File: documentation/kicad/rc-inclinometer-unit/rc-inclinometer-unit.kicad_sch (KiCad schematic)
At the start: 1 part

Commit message: kicad schema update
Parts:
- added SW?: SW_DIP_x01, symbol Switch:SW_DIP_x01
- added U?: Winch controller, symbol rc-inclinometer-unit-custom-library:Winch controller
- added U?: Logic Level Converter, symbol rc-inclinometer-unit-custom-library:Logic Level Converter
- added U?: Passive buzzer module, symbol rc-inclinometer-unit-custom-library:Passive buzzer module
- added U?: RC Receiver, symbol rc-inclinometer-unit-custom-library:RC Receiver
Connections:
- net at U?.12 (~{D9}): now also U?. (VCC)
- net at U?.4 (GND): now also SW?.2, U?. (LV4)
- net at U?.5 (D2): now also SW?.1
- net at U?.8 (~{D5}): now also U?. (LV4)
- net +5V: no longer names the net of U?.30 (VIN)
- net +5V: now also U?. (GND), U?. (VCC)
- net GND: no longer names the net of U?.29 (GND)
- net GND: now also U?. (GND), U?. (VCC), U?. (VCC)
- net IO: no longer names the net of U?.6 (~{D3})
- net IO: now also U?. (VCC)
- net VCC: no longer names the net of U?.17 (3V3)
- net VCC: now also U?. (LV4), U?. (VCC)
- new net: U?. (GND), U?. (LV4) (x3)
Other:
- note removed: "Passive buzzer module"
- note removed: "RC Receiver"

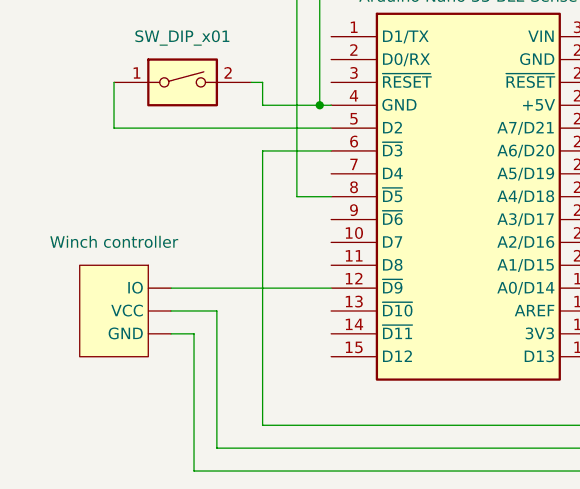
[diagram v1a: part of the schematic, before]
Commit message: front dig servo schema
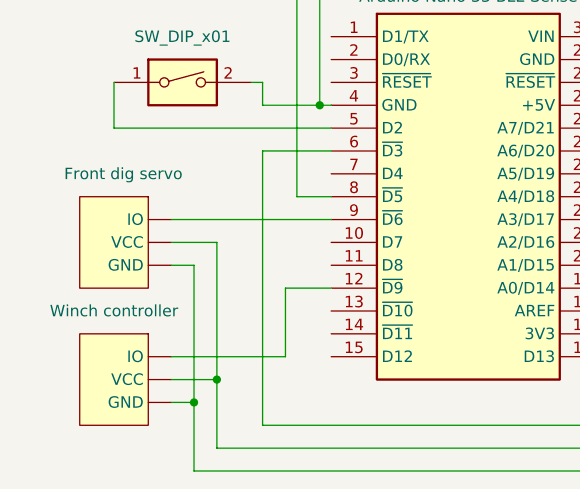
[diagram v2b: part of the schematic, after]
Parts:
- added U?: Front dig servo, symbol rc-inclinometer-unit-custom-library:Winch controller
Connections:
- net at U?. (GND), U?. (VCC), U?.30 (VIN): now also U?. (VCC)
- net at U?.9 (~{D6}): now also U?. (VCC)
- net at U?. (LV4): now also U?. (GND)
- net at U?. (GND): no longer U?. (LV4)
- new net: U?. (LV4), U?. (VCC), U?.17 (3V3)
- new net: U?. (GND), U?. (VCC), U?. (VCC), U?. (VCC), U?.29 (GND)
- new net: U?. (GND), U?. (LV4) (x2)
- now unconnected: U?. (GND), U?. (GND), U?. (GND)
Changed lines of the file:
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@@
   (junction (at 191.77 73.66) (diameter 0) (color 0 0 0 0)
   )
+  (junction (at 111.76 111.76) (diameter 0) (color 0 0 0 0)
+  )
   (junction (at 125.73 78.74) (diameter 0) (color 0 0 0 0)
   )
   (junction (at 189.23 71.12) (diameter 0) (color 0 0 0 0)
   )
+  (junction (at 114.3 109.22) (diameter 0) (color 0 0 0 0)
+  )
   (junction (at 161.29 104.14) (diameter 0) (color 0 0 0 0)
   )
@@
     (stroke (width 0) (type default) (color 0 0 0 0))
   )
-  (wire (pts (xy 109.22 101.6) (xy 114.3 101.6))
-    (stroke (width 0) (type default) (color 0 0 0 0))
-  )
   (wire (pts (xy 163.83 88.9) (xy 171.45 88.9))
     (stroke (width 0) (type default) (color 0 0 0 0))
@@
     (stroke (width 0) (type default) (color 0 0 0 0))
   )
-  (wire (pts (xy 114.3 101.6) (xy 114.3 116.84))
+  (wire (pts (xy 109.22 109.22) (xy 114.3 109.22))
+    (stroke (width 0) (type default) (color 0 0 0 0))
+  )
+  (wire (pts (xy 114.3 116.84) (xy 114.3 109.22))
+    (stroke (width 0) (type default) (color 0 0 0 0))
+  )
+  (wire (pts (xy 109.22 96.52) (xy 111.76 96.52))
     (stroke (width 0) (type default) (color 0 0 0 0))
   )
@@
     (stroke (width 0) (type default) (color 0 0 0 0))
   )
+  (wire (pts (xy 109.22 93.98) (xy 114.3 93.98))
+    (stroke (width 0) (type default) (color 0 0 0 0))
+  )
+  (wire (pts (xy 114.3 109.22) (xy 114.3 93.98))
+    (stroke (width 0) (type default) (color 0 0 0 0))
+  )
+  (wire (pts (xy 121.92 99.06) (xy 121.92 106.68))
+    (stroke (width 0) (type default) (color 0 0 0 0))
+  )
   (wire (pts (xy 191.77 73.66) (xy 193.04 73.66))
     (stroke (width 0) (type default) (color 0 0 0 0))
   )
+  (wire (pts (xy 127 99.06) (xy 121.92 99.06))
+    (stroke (width 0) (type default) (color 0 0 0 0))
+  )
   (wire (pts (xy 157.48 104.14) (xy 161.29 104.14))
     (stroke (width 0) (type default) (color 0 0 0 0))
@@
     (stroke (width 0) (type default) (color 0 0 0 0))
   )
-  (wire (pts (xy 109.22 104.14) (xy 111.76 104.14))
+  (wire (pts (xy 109.22 111.76) (xy 111.76 111.76))
     (stroke (width 0) (type default) (color 0 0 0 0))
   )
@@
     (stroke (width 0) (type default) (color 0 0 0 0))
   )
+  (wire (pts (xy 109.22 91.44) (xy 127 91.44))
+    (stroke (width 0) (type default) (color 0 0 0 0))
+  )
   (wire (pts (xy 189.23 55.88) (xy 182.88 55.88))
     (stroke (width 0) (type default) (color 0 0 0 0))
@@
     (stroke (width 0) (type default) (color 0 0 0 0))
   )
-  (wire (pts (xy 109.22 99.06) (xy 127 99.06))
-    (stroke (width 0) (type default) (color 0 0 0 0))
-  )
   (wire (pts (xy 191.77 60.96) (xy 191.77 50.8))
     (stroke (width 0) (type default) (color 0 0 0 0))
   )
-  (wire (pts (xy 111.76 104.14) (xy 111.76 119.38))
+  (wire (pts (xy 109.22 106.68) (xy 121.92 106.68))
+    (stroke (width 0) (type default) (color 0 0 0 0))
+  )
+  (wire (pts (xy 111.76 111.76) (xy 111.76 119.38))
+    (stroke (width 0) (type default) (color 0 0 0 0))
+  )
+  (wire (pts (xy 111.76 111.76) (xy 111.76 96.52))
     (stroke (width 0) (type default) (color 0 0 0 0))
   )
@@
     (pin "9")
   )
+  (symbol (lib_id "rc-inclinometer-unit-custom-library:Winch controller") (at 102.87 86.36 0) (mirror y) (unit 1)
+    (in_bom yes) (on_board yes)
+    (property "Reference" "U?" (id 0) (at 102.87 83.82 0)
+      (effects (font (size 1.27 1.27)) hide)
+    )
+    (property "Value" "Front dig servo" (id 1) (at 110.49 86.36 0)
+      (effects (font (size 1.27 1.27)) (justify left))
+    )
+    (property "Footprint" "" (id 2) (at 102.87 86.36 0)
+      (effects (font (size 1.27 1.27)) hide)
+    )
+    (property "Datasheet" "" (id 3) (at 102.87 86.36 0)
+      (effects (font (size 1.27 1.27)) hide)
+    )
+    (pin "")
+    (pin "")
+    (pin "")
+  )
   (symbol (lib_id "Switch:SW_DIP_x01") (at 110.49 76.2 0) (unit 1)
     (in_bom yes) (on_board yes) (fields_autoplaced)
@@
     (pin "2")
   )
-  (symbol (lib_id "rc-inclinometer-unit-custom-library:Winch controller") (at 102.87 93.98 0) (mirror y) (unit 1)
+  (symbol (lib_id "rc-inclinometer-unit-custom-library:Winch controller") (at 102.87 101.6 0) (mirror y) (unit 1)
     (in_bom yes) (on_board yes) (fields_autoplaced)
-    (property "Reference" "U?" (id 0) (at 102.87 91.44 0)
-      (effects (font (size 1.27 1.27)) hide)
-    )
-    (property "Value" "Winch controller" (id 1) (at 102.87 93.98 0))
-    (property "Footprint" "" (id 2) (at 102.87 93.98 0)
-      (effects (font (size 1.27 1.27)) hide)
-    )
-    (property "Datasheet" "" (id 3) (at 102.87 93.98 0)
+    (property "Reference" "U?" (id 0) (at 102.87 99.06 0)
+      (effects (font (size 1.27 1.27)) hide)
+    )
+    (property "Value" "Winch controller" (id 1) (at 102.87 101.6 0))
+    (property "Footprint" "" (id 2) (at 102.87 101.6 0)
+      (effects (font (size 1.27 1.27)) hide)
+    )
+    (property "Datasheet" "" (id 3) (at 102.87 101.6 0)
       (effects (font (size 1.27 1.27)) hide)
     )
@@
       (reference "U?") (unit 1) (value "Arduino Nano 33 BLE Sense") (footprint "Arduino:Arduino_Nano")
     )
+    (path "/2419fd11-7a3e-44cd-918f-8db3ea424502"
+      (reference "U?") (unit 1) (value "Front dig servo") (footprint "")
+    )
     (path "/7751ee78-6f34-4432-a4ed-c73af0d92627"

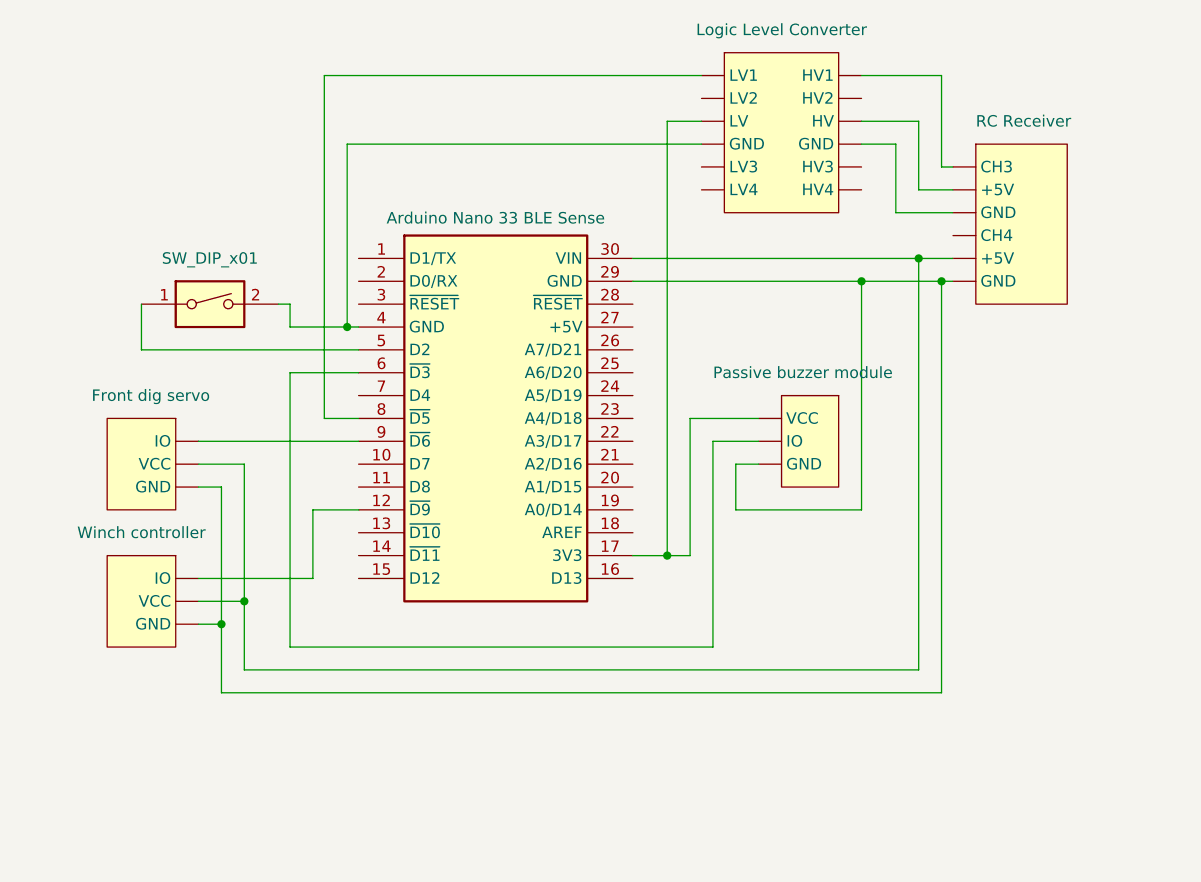
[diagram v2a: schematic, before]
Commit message: measure speed with hall effect sensor
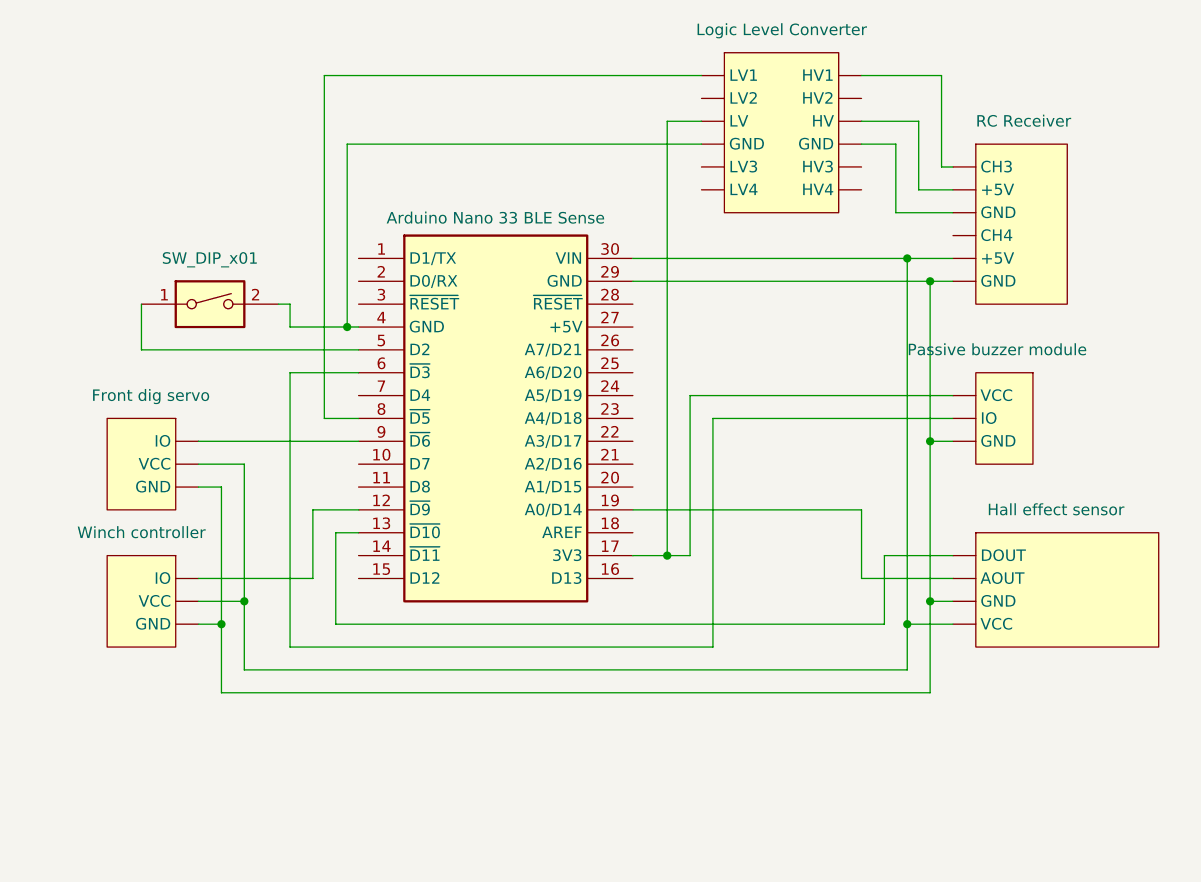
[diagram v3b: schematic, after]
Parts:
- added U?: Hall effect sensor, symbol rc-inclinometer-unit-custom-library:Hall effect sensor
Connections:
- net at U?.13 (~{D10}): now also U?. (VCC)
- net at U?.19 (A0/D14): now also U?. (VCC)
- net at U?. (GND), U?. (VCC), U?. (VCC)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: now also U?. (VCC)
- net at U?. (LV4): now also U?. (GND)
- net at U?. (GND): no longer U?. (LV4)
- new net: U?. (LV4), U?. (VCC), U?.17 (3V3)
- new net: U?. (GND), U?. (VCC), U?. (VCC), U?. (VCC), U?. (VCC), U?.29 (GND)
- new net: U?. (GND), U?. (LV4) (x2)
- now unconnected: U?. (GND), U?. (GND), U?. (GND)
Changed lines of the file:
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@@
 (kicad_sch (version 20211123) (generator eeschema)
   (paper "A4")
-  (junction (at 182.88 73.66) (diameter 0) (color 0 0 0 0)
-  )
-  (junction (at 191.77 73.66) (diameter 0) (color 0 0 0 0)
+  (junction (at 187.96 71.12) (diameter 0) (color 0 0 0 0)
   )
   (junction (at 111.76 111.76) (diameter 0) (color 0 0 0 0)
   )
+  (junction (at 190.5 73.66) (diameter 0) (color 0 0 0 0)
+  )
   (junction (at 125.73 78.74) (diameter 0) (color 0 0 0 0)
   )
-  (junction (at 189.23 71.12) (diameter 0) (color 0 0 0 0)
-  )
   (junction (at 114.3 109.22) (diameter 0) (color 0 0 0 0)
   )
+  (junction (at 187.96 111.76) (diameter 0) (color 0 0 0 0)
+  )
   (junction (at 161.29 104.14) (diameter 0) (color 0 0 0 0)
   )
+  (junction (at 190.5 109.22) (diameter 0) (color 0 0 0 0)
+  )
+  (junction (at 190.5 91.44) (diameter 0) (color 0 0 0 0)
+  )
+  (wire (pts (xy 157.48 99.06) (xy 182.88 99.06))
+    (stroke (width 0) (type default) (color 0 0 0 0))
+  )
   (wire (pts (xy 119.38 78.74) (xy 119.38 76.2))
     (stroke (width 0) (type default) (color 0 0 0 0))
   )
-  (wire (pts (xy 163.83 88.9) (xy 171.45 88.9))
-    (stroke (width 0) (type default) (color 0 0 0 0))
-  )
-  (wire (pts (xy 182.88 73.66) (xy 182.88 99.06))
-    (stroke (width 0) (type default) (color 0 0 0 0))
-  )
   (wire (pts (xy 182.88 50.8) (xy 191.77 50.8))
     (stroke (width 0) (type default) (color 0 0 0 0))
@@
     (stroke (width 0) (type default) (color 0 0 0 0))
   )
+  (wire (pts (xy 187.96 71.12) (xy 193.04 71.12))
+    (stroke (width 0) (type default) (color 0 0 0 0))
+  )
   (wire (pts (xy 161.29 104.14) (xy 163.83 104.14))
     (stroke (width 0) (type default) (color 0 0 0 0))
   )
-  (wire (pts (xy 189.23 71.12) (xy 193.04 71.12))
+  (wire (pts (xy 157.48 71.12) (xy 187.96 71.12))
+    (stroke (width 0) (type default) (color 0 0 0 0))
+  )
+  (wire (pts (xy 187.96 111.76) (xy 187.96 116.84))
+    (stroke (width 0) (type default) (color 0 0 0 0))
+  )
+  (wire (pts (xy 111.76 119.38) (xy 190.5 119.38))
     (stroke (width 0) (type default) (color 0 0 0 0))
   )
@@
     (stroke (width 0) (type default) (color 0 0 0 0))
   )
+  (wire (pts (xy 187.96 111.76) (xy 193.04 111.76))
+    (stroke (width 0) (type default) (color 0 0 0 0))
+  )
+  (wire (pts (xy 190.5 73.66) (xy 193.04 73.66))
+    (stroke (width 0) (type default) (color 0 0 0 0))
+  )
   (wire (pts (xy 109.22 96.52) (xy 111.76 96.52))
     (stroke (width 0) (type default) (color 0 0 0 0))
   )
-  (wire (pts (xy 189.23 71.12) (xy 189.23 116.84))
-    (stroke (width 0) (type default) (color 0 0 0 0))
-  )
-  (wire (pts (xy 191.77 73.66) (xy 191.77 119.38))
+  (wire (pts (xy 182.88 99.06) (xy 182.88 106.68))
+    (stroke (width 0) (type default) (color 0 0 0 0))
+  )
+  (wire (pts (xy 163.83 104.14) (xy 163.83 86.36))
     (stroke (width 0) (type default) (color 0 0 0 0))
   )
@@
     (stroke (width 0) (type default) (color 0 0 0 0))
   )
-  (wire (pts (xy 157.48 73.66) (xy 182.88 73.66))
-    (stroke (width 0) (type default) (color 0 0 0 0))
-  )
-  (wire (pts (xy 111.76 119.38) (xy 191.77 119.38))
+  (wire (pts (xy 166.37 114.3) (xy 166.37 88.9))
+    (stroke (width 0) (type default) (color 0 0 0 0))
+  )
+  (wire (pts (xy 190.5 91.44) (xy 190.5 109.22))
+    (stroke (width 0) (type default) (color 0 0 0 0))
+  )
+  (wire (pts (xy 124.46 101.6) (xy 124.46 111.76))
+    (stroke (width 0) (type default) (color 0 0 0 0))
+  )
+  (wire (pts (xy 190.5 73.66) (xy 190.5 91.44))
     (stroke (width 0) (type default) (color 0 0 0 0))
   )
@@
     (stroke (width 0) (type default) (color 0 0 0 0))
   )
-  (wire (pts (xy 114.3 116.84) (xy 189.23 116.84))
+  (wire (pts (xy 185.42 111.76) (xy 185.42 104.14))
+    (stroke (width 0) (type default) (color 0 0 0 0))
+  )
+  (wire (pts (xy 163.83 86.36) (xy 193.04 86.36))
     (stroke (width 0) (type default) (color 0 0 0 0))
   )
@@
     (stroke (width 0) (type default) (color 0 0 0 0))
   )
+  (wire (pts (xy 190.5 109.22) (xy 193.04 109.22))
+    (stroke (width 0) (type default) (color 0 0 0 0))
+  )
   (wire (pts (xy 123.19 88.9) (xy 123.19 50.8))
     (stroke (width 0) (type default) (color 0 0 0 0))
   )
-  (wire (pts (xy 166.37 91.44) (xy 171.45 91.44))
+  (wire (pts (xy 187.96 116.84) (xy 114.3 116.84))
+    (stroke (width 0) (type default) (color 0 0 0 0))
+  )
+  (wire (pts (xy 127 101.6) (xy 124.46 101.6))
     (stroke (width 0) (type default) (color 0 0 0 0))
   )
@@
     (stroke (width 0) (type default) (color 0 0 0 0))
   )
+  (wire (pts (xy 124.46 111.76) (xy 185.42 111.76))
+    (stroke (width 0) (type default) (color 0 0 0 0))
+  )
   (wire (pts (xy 114.3 109.22) (xy 114.3 93.98))
     (stroke (width 0) (type default) (color 0 0 0 0))
   )
+  (wire (pts (xy 190.5 109.22) (xy 190.5 119.38))
+    (stroke (width 0) (type default) (color 0 0 0 0))
+  )
   (wire (pts (xy 121.92 99.06) (xy 121.92 106.68))
     (stroke (width 0) (type default) (color 0 0 0 0))
   )
-  (wire (pts (xy 191.77 73.66) (xy 193.04 73.66))
+  (wire (pts (xy 157.48 73.66) (xy 190.5 73.66))
     (stroke (width 0) (type default) (color 0 0 0 0))
   )
@@
     (stroke (width 0) (type default) (color 0 0 0 0))
   )
+  (wire (pts (xy 187.96 71.12) (xy 187.96 111.76))
+    (stroke (width 0) (type default) (color 0 0 0 0))
+  )
+  (wire (pts (xy 190.5 91.44) (xy 193.04 91.44))
+    (stroke (width 0) (type default) (color 0 0 0 0))
+  )
+  (wire (pts (xy 185.42 104.14) (xy 193.04 104.14))
+    (stroke (width 0) (type default) (color 0 0 0 0))
+  )
   (wire (pts (xy 157.48 104.14) (xy 161.29 104.14))
     (stroke (width 0) (type default) (color 0 0 0 0))
   )
-  (wire (pts (xy 171.45 93.98) (xy 168.91 93.98))
-    (stroke (width 0) (type default) (color 0 0 0 0))
-  )
   (wire (pts (xy 109.22 111.76) (xy 111.76 111.76))
     (stroke (width 0) (type default) (color 0 0 0 0))
@@
     (stroke (width 0) (type default) (color 0 0 0 0))
   )
-  (wire (pts (xy 182.88 73.66) (xy 191.77 73.66))
+  (wire (pts (xy 166.37 88.9) (xy 193.04 88.9))
     (stroke (width 0) (type default) (color 0 0 0 0))
   )
@@
     (stroke (width 0) (type default) (color 0 0 0 0))
   )
+  (wire (pts (xy 193.04 106.68) (xy 182.88 106.68))
+    (stroke (width 0) (type default) (color 0 0 0 0))
+  )
   (wire (pts (xy 119.38 83.82) (xy 119.38 114.3))
     (stroke (width 0) (type default) (color 0 0 0 0))
   )
-  (wire (pts (xy 157.48 71.12) (xy 189.23 71.12))
-    (stroke (width 0) (type default) (color 0 0 0 0))
-  )
-  (wire (pts (xy 168.91 93.98) (xy 168.91 99.06))
-    (stroke (width 0) (type default) (color 0 0 0 0))
-  )
   (wire (pts (xy 123.19 88.9) (xy 127 88.9))
     (stroke (width 0) (type default) (color 0 0 0 0))
   )
-  (wire (pts (xy 168.91 99.06) (xy 182.88 99.06))
-    (stroke (width 0) (type default) (color 0 0 0 0))
-  )
-  (wire (pts (xy 166.37 114.3) (xy 166.37 91.44))
-    (stroke (width 0) (type default) (color 0 0 0 0))
-  )
   (wire (pts (xy 118.11 76.2) (xy 119.38 76.2))
     (stroke (width 0) (type default) (color 0 0 0 0))
   )
   (wire (pts (xy 182.88 58.42) (xy 186.69 58.42))
-    (stroke (width 0) (type default) (color 0 0 0 0))
-  )
-  (wire (pts (xy 163.83 104.14) (xy 163.83 88.9))
     (stroke (width 0) (type default) (color 0 0 0 0))
   )
@@
     (pin "")
   )
+  (symbol (lib_id "rc-inclinometer-unit-custom-library:Hall effect sensor") (at 205.74 99.06 0) (unit 1)
+    (in_bom yes) (on_board yes)
+    (property "Reference" "U?" (id 0) (at 217.17 106.6799 0)
+      (effects (font (size 1.27 1.27)) (justify left) hide)
+    )
+    (property "Value" "Hall effect sensor" (id 1) (at 196.85 99.06 0)
+      (effects (font (size 1.27 1.27)) (justify left))
+    )
+    (property "Footprint" "" (id 2) (at 205.74 99.06 0)
+      (effects (font (size 1.27 1.27)) hide)
+    )
+    (property "Datasheet" "" (id 3) (at 205.74 99.06 0)
+      (effects (font (size 1.27 1.27)) hide)
+    )
+    (pin "")
+    (pin "")
+    (pin "")
+    (pin "")
+  )
   (symbol (lib_id "Switch:SW_DIP_x01") (at 110.49 76.2 0) (unit 1)
     (in_bom yes) (on_board yes) (fields_autoplaced)
@@
     (pin "")
   )
-  (symbol (lib_id "rc-inclinometer-unit-custom-library:Passive buzzer module") (at 177.8 91.44 270) (unit 1)
-    (in_bom yes) (on_board yes)
-    (property "Reference" "U?" (id 0) (at 185.42 91.44 0)
-      (effects (font (size 1.27 1.27)) hide)
-    )
-    (property "Value" "Passive buzzer module" (id 1) (at 166.37 83.82 90)
+  (symbol (lib_id "rc-inclinometer-unit-custom-library:Passive buzzer module") (at 199.39 88.9 270) (unit 1)
+    (in_bom yes) (on_board yes)
+    (property "Reference" "U?" (id 0) (at 207.01 88.9 0)
+      (effects (font (size 1.27 1.27)) hide)
+    )
+    (property "Value" "Passive buzzer module" (id 1) (at 187.96 81.28 90)
       (effects (font (size 1.27 1.27)) (justify left))
     )
-    (property "Footprint" "" (id 2) (at 182.88 91.44 0)
-      (effects (font (size 1.27 1.27)) hide)
-    )
-    (property "Datasheet" "" (id 3) (at 182.88 91.44 0)
+    (property "Footprint" "" (id 2) (at 204.47 88.9 0)
+      (effects (font (size 1.27 1.27)) hide)
+    )
+    (property "Datasheet" "" (id 3) (at 204.47 88.9 0)
       (effects (font (size 1.27 1.27)) hide)
     )
@@
       (reference "U?") (unit 1) (value "Front dig servo") (footprint "")
     )
+    (path "/6a06bc5d-fa1a-4a1e-b574-cede84d86f64"
+      (reference "U?") (unit 1) (value "Hall effect sensor") (footprint "")
+    )
     (path "/7751ee78-6f34-4432-a4ed-c73af0d92627"
